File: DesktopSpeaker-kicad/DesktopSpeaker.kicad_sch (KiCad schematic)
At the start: 10 parts, among them J1 USB_C_Receptacle_USB2.0_16P, J2 HEAD_OUT, J3 AUX_IN, U1 BM83SM1-00TA, U2 PCM2902CDBR, U3 STM32G031K8T6, U4 BQ25895RTWR, U5 MAX17048G+T10, U6 TAS5825MRHBR, U7 TAS5825MRHBR

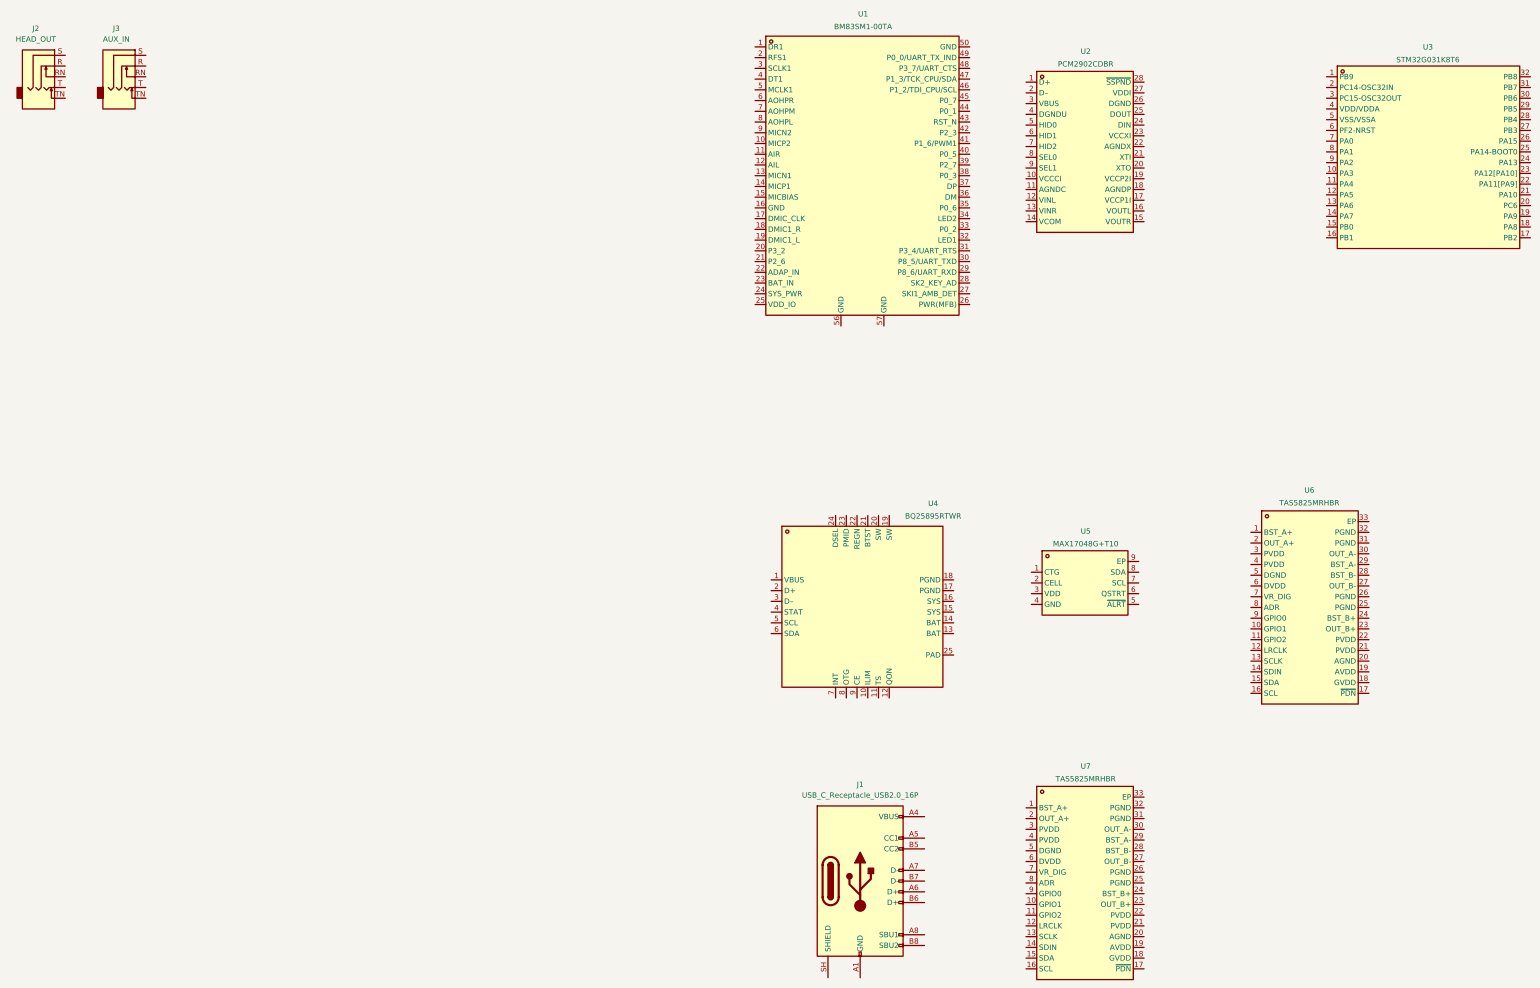
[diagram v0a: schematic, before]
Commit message: Capture and review speaker power subsystem schematics and libraries
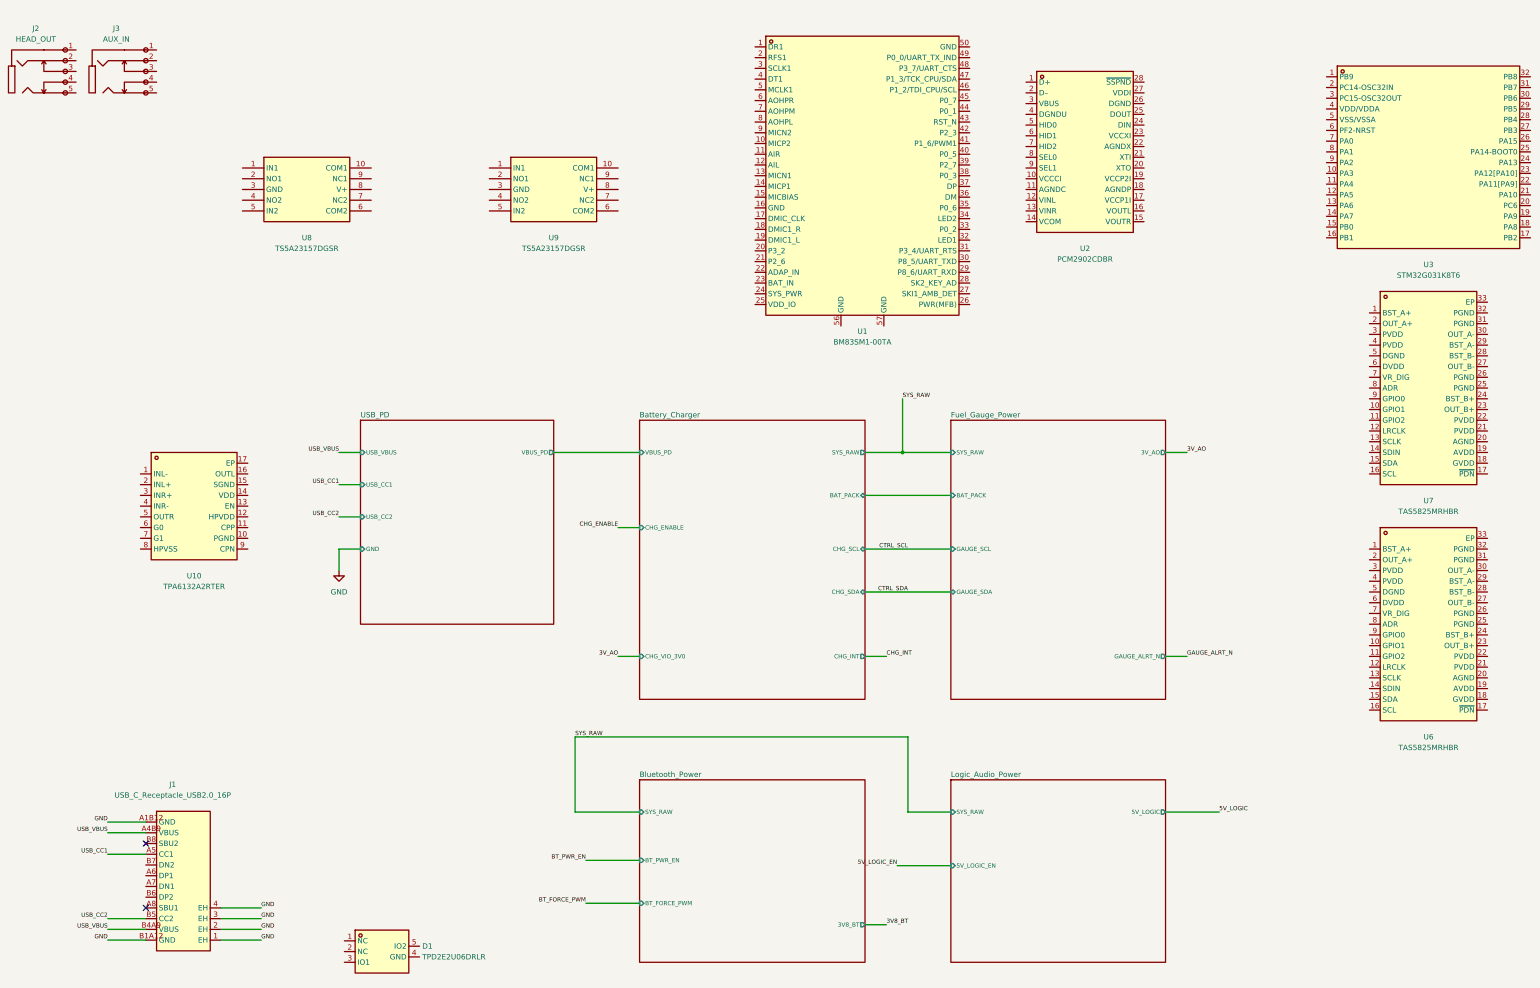
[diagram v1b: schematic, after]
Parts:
- removed U4: BQ25895RTWR, DesktopSpeaker:BQ25895RTWR, symbol BQ25895RTWR:BQ25895RTWR
- removed U5: MAX17048G+T10, DesktopSpeaker:MAX17048G+T10, symbol MAX17048G+T10:MAX17048G+T10
- added D1: TPD2E2U06DRLR, DesktopSpeaker:TPD2E2U06DRLR, symbol TPD2E2U06DRLR:TPD2E2U06DRLR
- added U10: TPA6132A2RTER, DesktopSpeaker:TPA6132A2RTER, symbol TPA6132A2RTER:TPA6132A2RTER
- added U8, U9: TS5A23157DGSR, DesktopSpeaker:TS5A23157DGSR, symbol TS5A23157DGSR:TS5A23157DGSR
- J1: footprint (none) -> DesktopSpeaker:TYPE-C-31-M-12; symbol Connector:USB_C_Receptacle_USB2.0_16P -> TYPE-C-31-M-12:TYPE-C-31-M-12; LCSC Part (none) -> C165948; MPN (none) -> TYPE-C-31-M-12; Manufacturer (none) -> Korean Hroparts
- J2, J3: footprint (none) -> DesktopSpeaker:PJ-307; symbol Connector_Audio:AudioJack3_SwitchTR -> PJ-307:PJ-307; LCSC Part (none) -> C2939173; MPN (none) -> PJ-307; Manufacturer (none) -> HOOYA
- U1: LCSC Part (none) -> C6752723; MPN (none) -> BM83SM1-00TA; Manufacturer (none) -> Microchip
- U2: LCSC Part (none) -> C2651869; MPN (none) -> PCM2902CDBR; Manufacturer (none) -> Texas Instruments
- U3: LCSC Part (none) -> C432203; MPN (none) -> STM32G031K8T6; Manufacturer (none) -> STMicroelectronics
- U6, U7: LCSC Part (none) -> C471049; MPN (none) -> TAS5825MRHBR; Manufacturer (none) -> Texas Instruments
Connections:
- net USB_CC1: now reaches J1.A5 (CC1)
- net USB_CC2: now reaches J1.B5 (CC2)
- new net GND: J1.1 (EH), J1.2 (EH), J1.3 (EH), J1.4 (EH), J1.A1B12 (GND), J1.B1A12 (GND)
- new net USB_VBUS: J1.A4B9 (VBUS), J1.B4A9 (VBUS)
- no-connect marks 0 -> 2
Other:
- added sheet Battery_Charger (Battery_Charger.kicad_sch)
- added sheet Bluetooth_Power (Bluetooth_Power.kicad_sch)
- added sheet Fuel_Gauge_Power (Fuel_Gauge_Power.kicad_sch)
- added sheet Logic_Audio_Power (Logic_Audio_Power.kicad_sch)
- added sheet USB_PD (USB_PD.kicad_sch)
- moved on the sheet: U6, U7

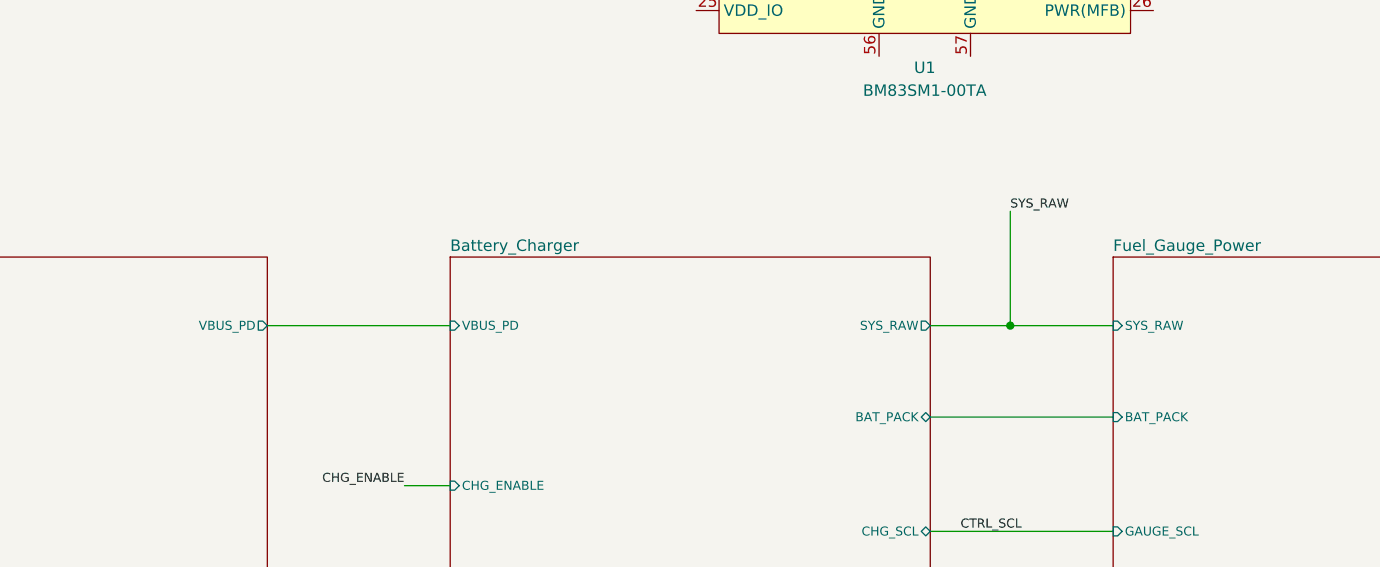
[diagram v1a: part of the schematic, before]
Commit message: Integrate USB auxiliary logic mux and reconcile active BOM
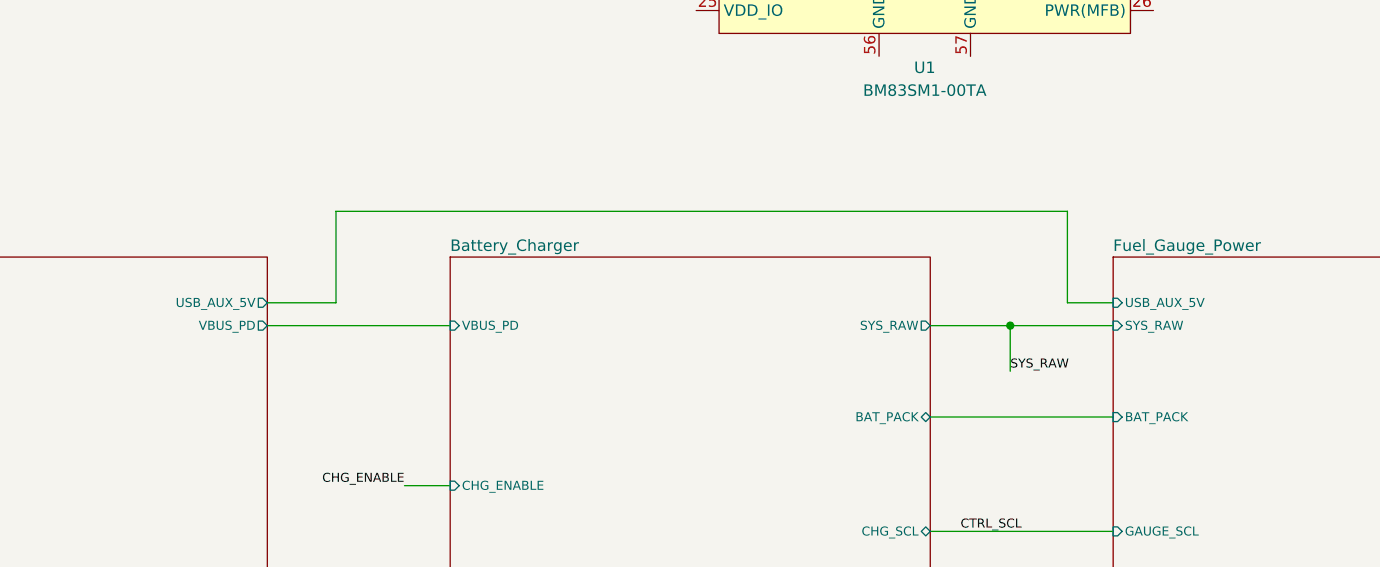
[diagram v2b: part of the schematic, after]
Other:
- sheet Fuel_Gauge_Power ports: added USB_AUX_5V; removed none
- sheet USB_PD ports: added USB_AUX_5V; removed none
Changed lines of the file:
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@@
 (no_connect (at 49.53 239.86))
 (no_connect (at 49.53 255.1))
-(sheet (at 100.33 139.7) (size 45.72 48.26) (stroke (width 0) (type default)) (fill (color 255 255 255 0)) (property "Sheet name" "USB_PD" (at 100.33 138.42999999999998 0) (effects (font (size 1.27 1.27)) (justify left))) (property "Sheet file" "USB_PD.kicad_sch" (at 100.33 187.95999999999998 0) (effects (font (size 1.27 1.27)) (hide yes))) (pin "USB_VBUS" input (at 100.33 147.32 180) (effects (font (size 1 1)) (justify left bottom))) (pin "USB_CC1" input (at 100.33 154.94 180) (effects (font (size 1 1)) (justify left bottom))) (pin "USB_CC2" input (at 100.33 162.56 180) (effects (font (size 1 1)) (justify left bottom))) (pin "GND" input (at 100.33 170.18 180) (effects (font (size 1 1)) (justify left bottom))) (pin "VBUS_PD" output (at 146.05 147.32 0) (effects (font (size 1 1)) (justify right bottom))) (instances (project "DesktopSpeaker" (path "/feda53ed-537d-4f88-9436-c6075776255b" (page "2")))))
+(sheet (at 100.33 139.7) (size 45.72 48.26) (stroke (width 0) (type default)) (fill (color 255 255 255 0)) (property "Sheet name" "USB_PD" (at 100.33 138.42999999999998 0) (effects (font (size 1.27 1.27)) (justify left))) (property "Sheet file" "USB_PD.kicad_sch" (at 100.33 187.95999999999998 0) (effects (font (size 1.27 1.27)) (hide yes))) (pin "USB_VBUS" input (at 100.33 147.32 180) (effects (font (size 1 1)) (justify left bottom))) (pin "USB_CC1" input (at 100.33 154.94 180) (effects (font (size 1 1)) (justify left bottom))) (pin "USB_CC2" input (at 100.33 162.56 180) (effects (font (size 1 1)) (justify left bottom))) (pin "GND" input (at 100.33 170.18 180) (effects (font (size 1 1)) (justify left bottom))) (pin "VBUS_PD" output (at 146.05 147.32 0) (effects (font (size 1 1)) (justify right bottom))) (instances (project "DesktopSpeaker" (path "/feda53ed-537d-4f88-9436-c6075776255b" (page "2")))) (pin "USB_AUX_5V" output (at 146.05 144.78 0) (effects (font (size 1 1)) (justify right bottom))))
 (sheet (at 166.37 139.7) (size 53.34 66.04) (stroke (width 0) (type default)) (fill (color 255 255 255 0)) (property "Sheet name" "Battery_Charger" (at 166.37 138.42999999999998 0) (effects (font (size 1.27 1.27)) (justify left))) (property "Sheet file" "Battery_Charger.kicad_sch" (at 166.37 205.74 0) (effects (font (size 1.27 1.27)) (hide yes))) (pin "VBUS_PD" input (at 166.37 147.32 180) (effects (font (size 1 1)) (justify left bottom))) (pin "CHG_ENABLE" input (at 166.37 165.1 180) (effects (font (size 1 1)) (justify left bottom))) (pin "CHG_VIO_3V0" input (at 166.37 195.58 180) (effects (font (size 1 1)) (justify left bottom))) (pin "SYS_RAW" output (at 219.71 147.32 0) (effects (font (size 1 1)) (justify right bottom))) (pin "BAT_PACK" bidirectional (at 219.71 157.48 0) (effects (font (size 1 1)) (justify right bottom))) (pin "CHG_SCL" bidirectional (at 219.71 170.18 0) (effects (font (size 1 1)) (justify right bottom))) (pin "CHG_SDA" bidirectional (at 219.71 180.34 0) (effects (font (size 1 1)) (justify right bottom))) (pin "CHG_INT" output (at 219.71 195.58 0) (effects (font (size 1 1)) (justify right bottom))) (instances (project "DesktopSpeaker" (path "/feda53ed-537d-4f88-9436-c6075776255b" (page "3")))))
-(sheet (at 240.03 139.7) (size 50.8 66.04) (stroke (width 0) (type default)) (fill (color 255 255 255 0)) (property "Sheet name" "Fuel_Gauge_Power" (at 240.03 138.42999999999998 0) (effects (font (size 1.27 1.27)) (justify left))) (property "Sheet file" "Fuel_Gauge_Power.kicad_sch" (at 240.03 205.74 0) (effects (font (size 1.27 1.27)) (hide yes))) (pin "SYS_RAW" input (at 240.03 147.32 180) (effects (font (size 1 1)) (justify left bottom))) (pin "BAT_PACK" input (at 240.03 157.48 180) (effects (font (size 1 1)) (justify left bottom))) (pin "GAUGE_SCL" input (at 240.03 170.18 180) (effects (font (size 1 1)) (justify left bottom))) (pin "GAUGE_SDA" bidirectional (at 240.03 180.34 180) (effects (font (size 1 1)) (justify left bottom))) (pin "3V_AO" output (at 290.83 147.32 0) (effects (font (size 1 1)) (justify right bottom))) (pin "GAUGE_ALRT_N" output (at 290.83 195.58 0) (effects (font (size 1 1)) (justify right bottom))) (instances (project "DesktopSpeaker" (path "/feda53ed-537d-4f88-9436-c6075776255b" (page "4")))))
+(sheet (at 240.03 139.7) (size 50.8 66.04) (stroke (width 0) (type default)) (fill (color 255 255 255 0)) (property "Sheet name" "Fuel_Gauge_Power" (at 240.03 138.42999999999998 0) (effects (font (size 1.27 1.27)) (justify left))) (property "Sheet file" "Fuel_Gauge_Power.kicad_sch" (at 240.03 205.74 0) (effects (font (size 1.27 1.27)) (hide yes))) (pin "SYS_RAW" input (at 240.03 147.32 180) (effects (font (size 1 1)) (justify left bottom))) (pin "BAT_PACK" input (at 240.03 157.48 180) (effects (font (size 1 1)) (justify left bottom))) (pin "GAUGE_SCL" input (at 240.03 170.18 180) (effects (font (size 1 1)) (justify left bottom))) (pin "GAUGE_SDA" bidirectional (at 240.03 180.34 180) (effects (font (size 1 1)) (justify left bottom))) (pin "3V_AO" output (at 290.83 147.32 0) (effects (font (size 1 1)) (justify right bottom))) (pin "GAUGE_ALRT_N" output (at 290.83 195.58 0) (effects (font (size 1 1)) (justify right bottom))) (instances (project "DesktopSpeaker" (path "/feda53ed-537d-4f88-9436-c6075776255b" (page "4")))) (pin "USB_AUX_5V" input (at 240.03 144.78 180) (effects (font (size 1 1)) (justify left bottom))))
 (wire (pts (xy 146.05 147.32) (xy 166.37 147.32)) (stroke (width 0) (type default)))
 (wire (pts (xy 219.71 147.32) (xy 240.03 147.32)) (stroke (width 0) (type default)))
@@
 (sheet (at 166.37 224.79) (size 53.34 43.18) (stroke (width 0) (type default)) (fill (color 255 255 255 0)) (property "Sheet name" "Bluetooth_Power" (at 166.37 223.51999999999998 0) (effects (font (size 1.27 1.27)) (justify left))) (property "Sheet file" "Bluetooth_Power.kicad_sch" (at 166.37 267.96999999999997 0) (effects (font (size 1.27 1.27)) (hide yes))) (pin "SYS_RAW" input (at 166.37 232.41 180) (effects (font (size 1 1)) (justify left bottom))) (pin "BT_PWR_EN" input (at 166.37 243.84 180) (effects (font (size 1 1)) (justify left bottom))) (pin "BT_FORCE_PWM" input (at 166.37 254.0 180) (effects (font (size 1 1)) (justify left bottom))) (pin "3V8_BT" output (at 219.71 259.08 0) (effects (font (size 1 1)) (justify right bottom))) (instances (project "DesktopSpeaker" (path "/feda53ed-537d-4f88-9436-c6075776255b" (page "5")))))
 (sheet (at 240.03 224.79) (size 50.8 43.18) (stroke (width 0) (type default)) (fill (color 255 255 255 0)) (property "Sheet name" "Logic_Audio_Power" (at 240.03 223.51999999999998 0) (effects (font (size 1.27 1.27)) (justify left))) (property "Sheet file" "Logic_Audio_Power.kicad_sch" (at 240.03 267.96999999999997 0) (effects (font (size 1.27 1.27)) (hide yes))) (pin "SYS_RAW" input (at 240.03 232.41 180) (effects (font (size 1 1)) (justify left bottom))) (pin "5V_LOGIC_EN" input (at 240.03 245.11 180) (effects (font (size 1 1)) (justify left bottom))) (pin "5V_LOGIC" output (at 290.83 232.41 0) (effects (font (size 1 1)) (justify right bottom))) (instances (project "DesktopSpeaker" (path "/feda53ed-537d-4f88-9436-c6075776255b" (page "6")))))
-(wire (pts (xy 228.6 147.32) (xy 228.6 134.62)) (stroke (width 0) (type default)))
-(label "SYS_RAW" (at 228.6 134.62 0) (effects (font (size 1 1)) (justify left bottom)))
+(wire (pts (xy 228.6 147.32) (xy 228.6 152.4)) (stroke (width 0) (type default)))
+(label "SYS_RAW" (at 228.6 152.4 0) (effects (font (size 1 1)) (justify left bottom)))
 (junction (at 228.6 147.32) (diameter 0) (color 0 0 0 0))
 (wire (pts (xy 151.13 214.63) (xy 229.87 214.63)) (stroke (width 0) (type default)))
@@
 (wire (pts (xy 290.83 232.41) (xy 303.53 232.41)) (stroke (width 0) (type default)))
 (label "5V_LOGIC" (at 303.53 232.41 0) (effects (font (size 1 1)) (justify left bottom)))
-)
+(wire (pts (xy 146.05 144.78) (xy 153.67 144.78)) (stroke (width 0) (type default)))
+(wire (pts (xy 153.67 144.78) (xy 153.67 134.62)) (stroke (width 0) (type default)))
+(wire (pts (xy 153.67 134.62) (xy 234.95 134.62)) (stroke (width 0) (type default)))
+(wire (pts (xy 234.95 134.62) (xy 234.95 144.78)) (stroke (width 0) (type default)))
+(wire (pts (xy 234.95 144.78) (xy 240.03 144.78)) (stroke (width 0) (type default))))
